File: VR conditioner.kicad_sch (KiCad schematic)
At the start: 15 parts, among them U10 MAX9924

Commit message: BOM cleanup, minor USB improvements, bump to 1.2
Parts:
- C23, C24, C25, R25, R26, R27, R28, R30, R31, R34: LCSC_ext 0 -> (none)
- R29: value DNP -> ~; LCSC DNP -> (none); now not fitted
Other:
- company: FutureProofPerformance.com -> github.com/FOME-Tech
- title: Polygonus Universal 88p -> FOME Universal 112 pin ECU base
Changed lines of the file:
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@@
 	(paper "A4")
 	(title_block
-		(title "Polygonus Universal 88p")
-		(date "2023-11-12")
-		(rev "v1.0")
-		(company "FutureProofPerformance.com")
+		(title "FOME Universal 112 pin ECU base")
+		(date "2026-03-03")
+		(rev "v1.2")
+		(company "github.com/FOME-Tech")
+		(comment 1 "FutureProofPerformance.com")
+		(comment 2 "happycactusgarage.com")
 	)
 	(text "Optional setting in Mode C for no adaptive threshold timeout - See MAX9924 Datasheet\nComponents as specified put chip in mode A1.  Flip jumper and install R1219+R2020 for mode C."
@@
 			)
 		)
-		(property "LCSC_ext" "0"
-			(at 103.505 80.01 0)
-			(effects
-				(font
-					(size 1.27 1.27)
-				)
-				(hide yes)
-			)
-		)
 		(pin "1"
 		)
@@
 			)
 		)
-		(property "LCSC_ext" "0"
-			(at 118.11 85.09 0)
-			(effects
-				(font
-					(size 1.27 1.27)
-				)
-				(hide yes)
-			)
-		)
 		(pin "1"
 		)
@@
 			)
 		)
-		(property "LCSC_ext" "0"
-			(at 113.03 90.17 0)
-			(effects
-				(font
-					(size 1.27 1.27)
-				)
-				(hide yes)
-			)
-		)
 		(pin "1"
 		)
@@
 		(in_bom yes)
 		(on_board yes)
-		(dnp no)
+		(dnp yes)
 		(property "Reference" "R29"
 			(at 130.9878 85.09 90)
@@
 			)
 		)
-		(property "Value" "DNP"
+		(property "Value" "~"
 			(at 125.73 85.09 90)
 			(effects
@@
 			)
 		)
-		(property "LCSC" "DNP"
+		(property "LCSC" ""
 			(at 125.73 85.09 0)
 			(effects
@@
 			)
 		)
-		(property "LCSC_ext" "0"
-			(at 127 97.79 0)
-			(effects
-				(font
-					(size 1.27 1.27)
-				)
-				(hide yes)
-			)
-		)
 		(pin "1"
 		)
@@
 		)
 		(property "LCSC" "C17673"
-			(at 165.735 79.375 0)
-			(effects
-				(font
-					(size 1.27 1.27)
-				)
-				(hide yes)
-			)
-		)
-		(property "LCSC_ext" "0"
 			(at 165.735 79.375 0)
 			(effects
@@
 			)
 		)
-		(property "LCSC_ext" "0"
-			(at 127 109.855 0)
-			(effects
-				(font
-					(size 1.27 1.27)
-				)
-				(hide yes)
-			)
-		)
 		(pin "1"
 		)
@@
 			)
 		)
-		(property "LCSC_ext" "0"
-			(at 188.595 103.505 0)
-			(effects
-				(font
-					(size 1.27 1.27)
-				)
-				(hide yes)
-			)
-		)
 		(pin "1"
 		)
@@
 			)
 		)
-		(property "LCSC_ext" "0"
-			(at 103.505 90.17 0)
-			(effects
-				(font
-					(size 1.27 1.27)
-				)
-				(hide yes)
-			)
-		)
 		(pin "1"
 		)
@@
 			)
 		)
-		(property "LCSC_ext" "0"
-			(at 127 103.505 0)
-			(effects
-				(font
-					(size 1.27 1.27)
-				)
-				(hide yes)
-			)
-		)
 		(pin "1"
 		)
@@
 			(at 113.03 80.01 0)
 			(effects
-				(font
-					(size 1.27 1.27)
-				)
-				(hide yes)
-			)
-		)
-		(property "LCSC_ext" "0"
-			(at 113.03 80.01 0)
-			(effects

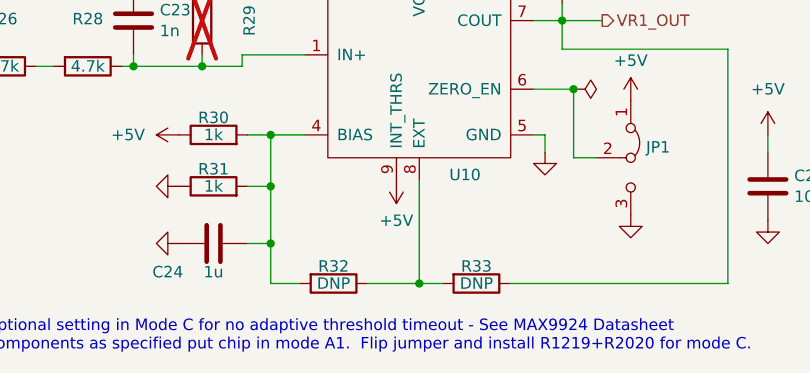
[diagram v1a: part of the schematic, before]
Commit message: more BOM optimization
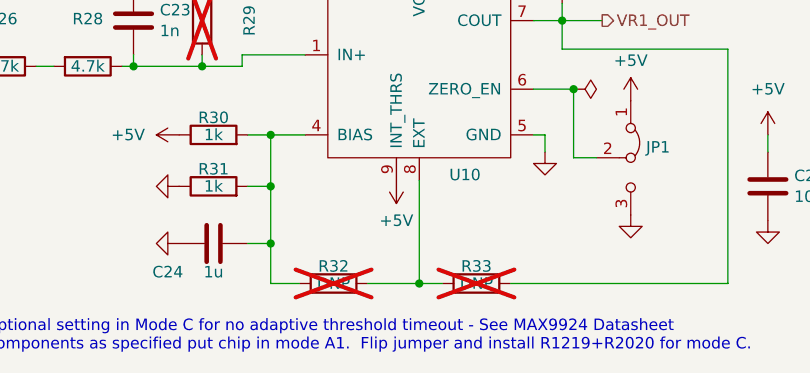
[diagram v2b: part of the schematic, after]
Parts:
- C25: footprint Capacitor_SMD:C_0805_2012Metric_Pad1.18x1.45mm_HandSolder -> Capacitor_SMD:C_0402_1005Metric; LCSC C28323 -> C1525
- JP1, R29: now left out of the parts list
- R32, R33: now not fitted; now left out of the parts list
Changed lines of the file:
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@@
 		(unit 1)
 		(exclude_from_sim no)
-		(in_bom yes)
+		(in_bom no)
 		(on_board yes)
 		(dnp no)
@@
 		(unit 1)
 		(exclude_from_sim no)
-		(in_bom yes)
+		(in_bom no)
 		(on_board yes)
 		(dnp yes)
@@
 		(unit 1)
 		(exclude_from_sim no)
-		(in_bom yes)
-		(on_board yes)
-		(dnp no)
+		(in_bom no)
+		(on_board yes)
+		(dnp yes)
 		(property "Reference" "R32"
 			(at 140.335 112.395 90)
@@
 			)
 		)
-		(property "Footprint" "Capacitor_SMD:C_0805_2012Metric_Pad1.18x1.45mm_HandSolder"
+		(property "Footprint" "Capacitor_SMD:C_0402_1005Metric"
 			(at 189.5602 107.315 0)
 			(effects
@@
 			)
 		)
-		(property "LCSC" "C28323"
+		(property "LCSC" "C1525"
 			(at 188.595 103.505 0)
 			(effects
@@
 		(unit 1)
 		(exclude_from_sim no)
-		(in_bom yes)
-		(on_board yes)
-		(dnp no)
+		(in_bom no)
+		(on_board yes)
+		(dnp yes)
 		(property "Reference" "R33"
 			(at 156.21 112.395 90)
